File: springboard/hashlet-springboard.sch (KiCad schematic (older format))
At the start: 3 parts, among them K1 CONN_3, P1 CONN_7X2, U1 ATSHA204A

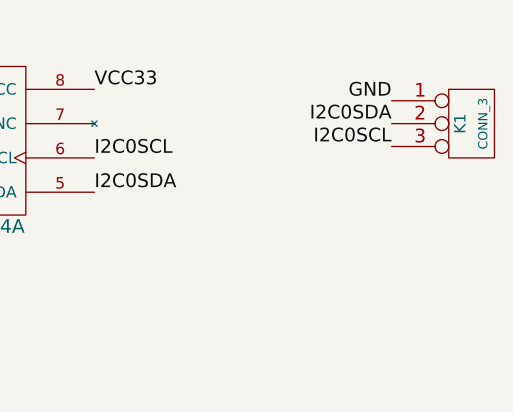
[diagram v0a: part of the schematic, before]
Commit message: springboard: PCB preparation v1
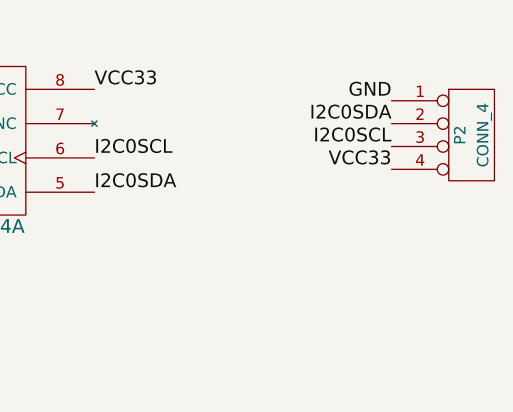
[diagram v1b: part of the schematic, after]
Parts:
- removed K1: CONN_3, ~, symbol CONN_3
- added P2: CONN_4, ~, symbol CONN_4
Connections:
- net GND: now also P2.1 (P1)
- net I2C0SCL: now also P2.3 (P3)
- net I2C0SDA: now also P2.2 (P2)
- net VCC33: now also P2.4 (P4)
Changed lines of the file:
@@
 LIBS:valves
 LIBS:crypto
+LIBS:hashlet-springboard-cache
 EELAYER 27 0
 EELAYER END
@@
 Sheet 1 1
 Title "Hashlet for VIA Springboard"
-Date "16 nov 2014"
+Date "9 dec 2014"
 Rev "1"
 Comp "Gergely Imreh / Moonpunch"
@@
 F 3 "~" H 5650 4800 60  0000 C CNN
 	1    5650 4800
-	1    0    0    -1
-$EndComp
-$Comp
-L CONN_3 K1
-U 1 1 5468604F
-P 7800 4750
-F 0 "K1" V 7750 4750 50  0000 C CNN
-F 1 "CONN_3" V 7850 4750 40  0000 C CNN
-F 2 "~" H 7800 4750 60  0000 C CNN
-F 3 "~" H 7800 4750 60  0000 C CNN
-	1    7800 4750
 	1    0    0    -1
 $EndComp
@@
 I2C0SCL
 $Comp
-L PWR_FLAG #FLG01
+L PWR_FLAG #FLG1
 U 1 1 546861FB
 P 3150 4500
-F 0 "#FLG01" H 3150 4595 30  0001 C CNN
+F 0 "#FLG1" H 3150 4595 30  0001 C CNN
 F 1 "PWR_FLAG" H 3150 4680 30  0000 C CNN
 F 2 "" H 3150 4500 60  0000 C CNN
@@
 $EndComp
 $Comp
-L GND #PWR02
+L GND #PWR1
 U 1 1 5468620A
 P 3400 5550
-F 0 "#PWR02" H 3400 5550 30  0001 C CNN
+F 0 "#PWR1" H 3400 5550 30  0001 C CNN
 F 1 "GND" H 3400 5480 30  0001 C CNN
 F 2 "" H 3400 5550 60  0000 C CNN
@@
 $EndComp
 $Comp
-L PWR_FLAG #FLG03
+L PWR_FLAG #FLG2
 U 1 1 54686219
 P 3550 5500
-F 0 "#FLG03" H 3550 5595 30  0001 C CNN
+F 0 "#FLG2" H 3550 5595 30  0001 C CNN
 F 1 "PWR_FLAG" H 3550 5680 30  0000 C CNN
 F 2 "" H 3550 5500 60  0000 C CNN
@@
 Text Notes 2950 6950 0    60   ~ 0
 Based on Cryptotronix's version of the original Hashlet\nSee source at https://github.com/cryptotronix/hashlet
+$Comp
+L CONN_4 P2
+U 1 1 54871099
+P 7800 4800
+F 0 "P2" V 7750 4800 50  0000 C CNN
+F 1 "CONN_4" V 7850 4800 50  0000 C CNN
+F 2 "~" H 7800 4800 60  0000 C CNN
+F 3 "~" H 7800 4800 60  0000 C CNN
+	1    7800 4800
+	1    0    0    -1
+$EndComp
+Text Label 7450 4950 2    60   ~ 0
+VCC33
 $EndSCHEMATC

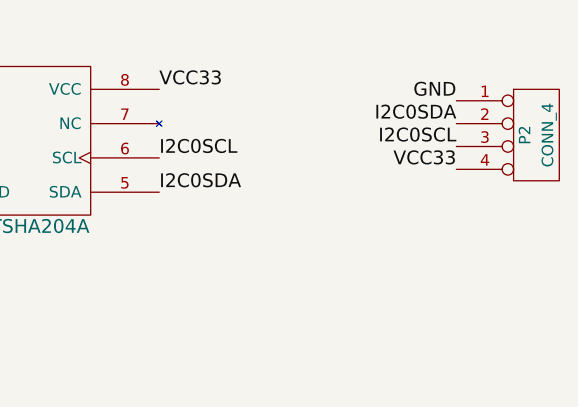
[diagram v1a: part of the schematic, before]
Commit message: springboard: adjusted wiring before submission to manufacturing
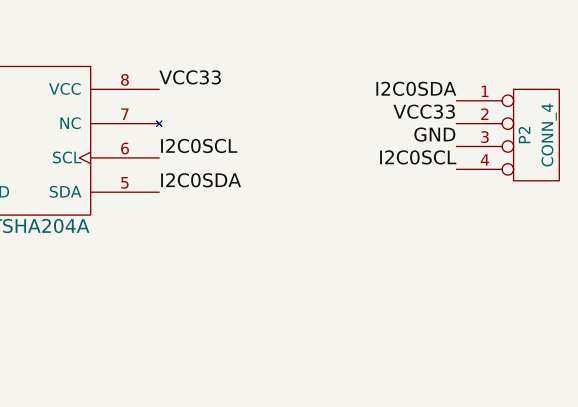
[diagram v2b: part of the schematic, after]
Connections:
- net GND: now also P2.3 (P3); no longer P2.1 (P1)
- net I2C0SCL: now also P2.4 (P4); no longer P2.3 (P3)
- net I2C0SDA: now also P2.1 (P1); no longer P2.2 (P2)
- net VCC33: now also P2.2 (P2); no longer P2.4 (P4)
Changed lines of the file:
@@
 Sheet 1 1
 Title "Hashlet for VIA Springboard"
-Date "9 dec 2014"
+Date "10 dec 2014"
 Rev "1"
 Comp "Gergely Imreh / Moonpunch"
@@
 Text Label 5000 5050 2    60   ~ 0
 GND
+Text Label 7450 4850 2    60   ~ 0
+GND
 Text Label 7450 4650 2    60   ~ 0
-GND
-Text Label 7450 4750 2    60   ~ 0
 I2C0SDA
-Text Label 7450 4850 2    60   ~ 0
+Text Label 7450 4950 2    60   ~ 0
 I2C0SCL
 $Comp
-L PWR_FLAG #FLG1
+L PWR_FLAG #FLG01
 U 1 1 546861FB
 P 3150 4500
-F 0 "#FLG1" H 3150 4595 30  0001 C CNN
+F 0 "#FLG01" H 3150 4595 30  0001 C CNN
 F 1 "PWR_FLAG" H 3150 4680 30  0000 C CNN
 F 2 "" H 3150 4500 60  0000 C CNN
@@
 $EndComp
 $Comp
-L GND #PWR1
+L GND #PWR02
 U 1 1 5468620A
 P 3400 5550
-F 0 "#PWR1" H 3400 5550 30  0001 C CNN
+F 0 "#PWR02" H 3400 5550 30  0001 C CNN
 F 1 "GND" H 3400 5480 30  0001 C CNN
 F 2 "" H 3400 5550 60  0000 C CNN
@@
 $EndComp
 $Comp
-L PWR_FLAG #FLG2
+L PWR_FLAG #FLG03
 U 1 1 54686219
 P 3550 5500
-F 0 "#FLG2" H 3550 5595 30  0001 C CNN
+F 0 "#FLG03" H 3550 5595 30  0001 C CNN
 F 1 "PWR_FLAG" H 3550 5680 30  0000 C CNN
 F 2 "" H 3550 5500 60  0000 C CNN
@@
 	1    0    0    -1
 $EndComp
-Text Label 7450 4950 2    60   ~ 0
+Text Label 7450 4750 2    60   ~ 0
 VCC33
 $EndSCHEMATC
